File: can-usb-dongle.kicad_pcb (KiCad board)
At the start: 2 copper layers, 30 x 15 mm, 43 parts, among them SW1 SW_PUSH, U1 STM32F302C8T, U2 SN65HVD256, U3 NUF2042XV6, U4 MCP1700, U5 SiP32431, X1 16MHz 10ppm

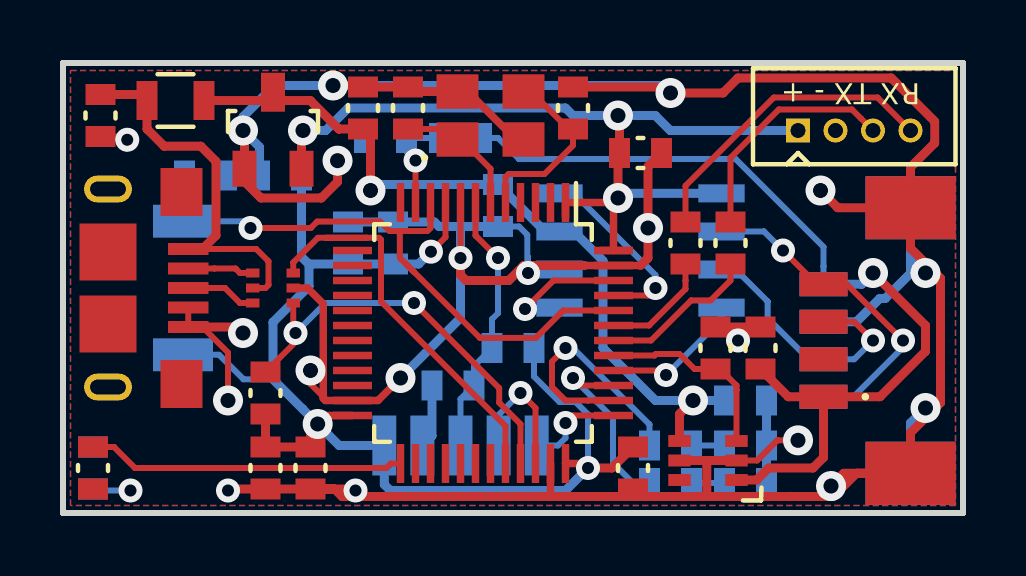
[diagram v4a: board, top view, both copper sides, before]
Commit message: Resolve JTAG pin conflict, add V_BUS_SENSE filter cap
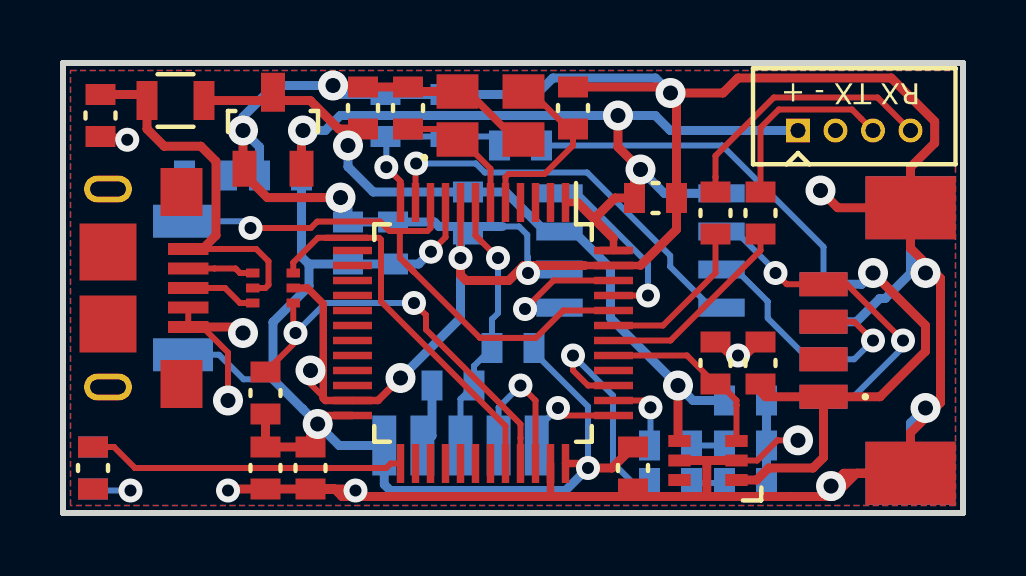
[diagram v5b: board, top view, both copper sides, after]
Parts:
- added C16: 100nF, _std:_0603, B.Cu at (57.8, 39.2)
- moved R3 2.02 mm to (60.2, 40.2)
- moved C3 1.58 mm to (64.8, 42.0)
- moved R10 1.41 mm to (66.8, 42.5)
- moved R11 1.41 mm to (68.2, 42.5)
- moved C9 1.03 mm to (58.5, 42.5)
- moved R4 0.75 mm to (55.8, 39.2), turned to 90 degrees
- moved C14 0.50 mm to (68.2, 47.5)
- moved R9 0.50 mm to (66.8, 47.5)
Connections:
- U1 pad 11: /V_BUS_SENSE -> /CAN_SILENT
- U1 pad 12: Net-(U1-Pad12) -> /V_BUS_SENSE
- U1 pad 40: /CAN_SILENT -> Net-(U1-Pad40)
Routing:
- net /CAN_SILENT: track 4.82 -> 13.7 mm
- net /CAN1_PWR_LED: track 8.28 -> 2.61 mm
- net /V_BUS_SENSE: track 3.37 -> 6.33 mm
- net /V_CAN_BUS: track 32.1 -> 29.7 mm
- net GND: track 158.5 -> 160.9 mm, vias 20 -> 19
- net /UART1_RX: track 3.74 -> 5.42 mm
- net Net-(CONN1-Pad4): track 10.4 -> 8.97 mm
- net /UART1_TX: track 5.28 -> 6.69 mm
- net Net-(CONN1-Pad3): track 7.85 -> 6.43 mm
- net /CAN1_STATUS_LED: track 6.33 -> 7.69 mm
- net /SWDIO: track 4.61 -> 5.11 mm

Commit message: Fix silkscreen text
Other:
- board text added: "CAN to USB RevA"
- board text removed: "CVRA CAN to USB dongle Rev A"
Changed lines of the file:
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@@
     (area 44.899999 37.399999 75.100001 52.600001)
     (thickness 1.6)
-    (drawings 21)
+    (drawings 23)
     (tracks 487)
     (zones 0)
@@
   )
   (setup
-    (last_trace_width 0.3)
+    (last_trace_width 0.2)
     (user_trace_width 0.1524)
     (user_trace_width 0.1524)
@@
       (net 2 GND))
   )
+  (gr_text + (at 69 49.25) (layer F.SilkS)
+    (effects (font (size 1 1) (thickness 0.2)))
+  )
+  (gr_text + (at 69.25 43.75) (layer B.SilkS)
+    (effects (font (size 1 1) (thickness 0.2)) (justify mirror))
+  )
   (gr_line (start 46.3 51.15) (end 45.7 51.15) (layer B.SilkS) (width 0.15))
   (gr_line (start 46 50.85) (end 46.3 51.15) (layer B.SilkS) (width 0.15))
@@
     (effects (font (size 0.8 0.8) (thickness 0.2)) (justify mirror))
   )
-  (gr_text "CVRA CAN to USB dongle Rev A" (at 45.75 38.75 180) (layer B.SilkS)
+  (gr_text "CAN to USB           RevA" (at 45.75 38.75 180) (layer B.SilkS)
     (effects (font (size 0.8 0.8) (thickness 0.15)) (justify left mirror))
   )

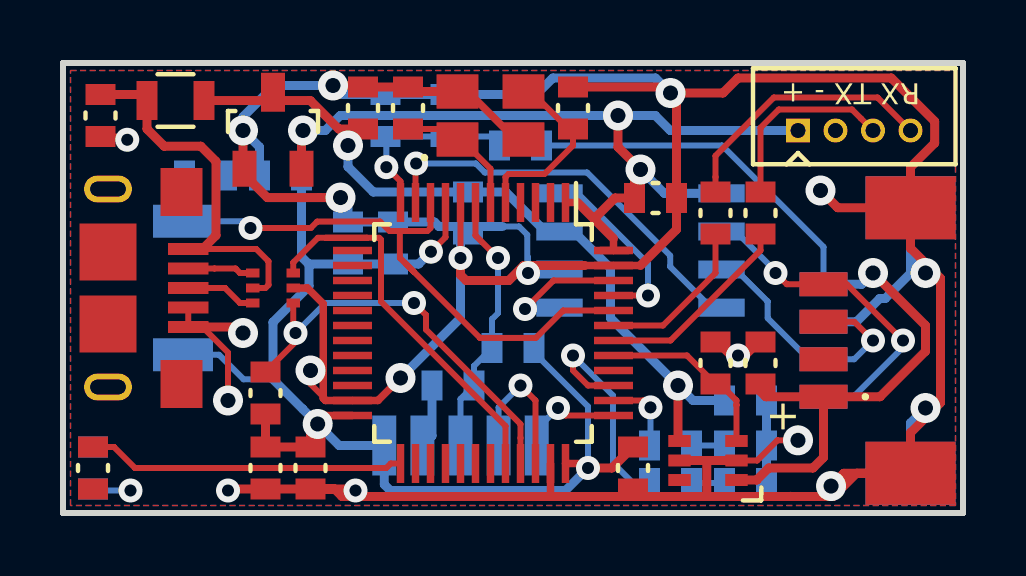
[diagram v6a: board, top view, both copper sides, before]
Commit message: Increase component dinstance on backside for handsoldering
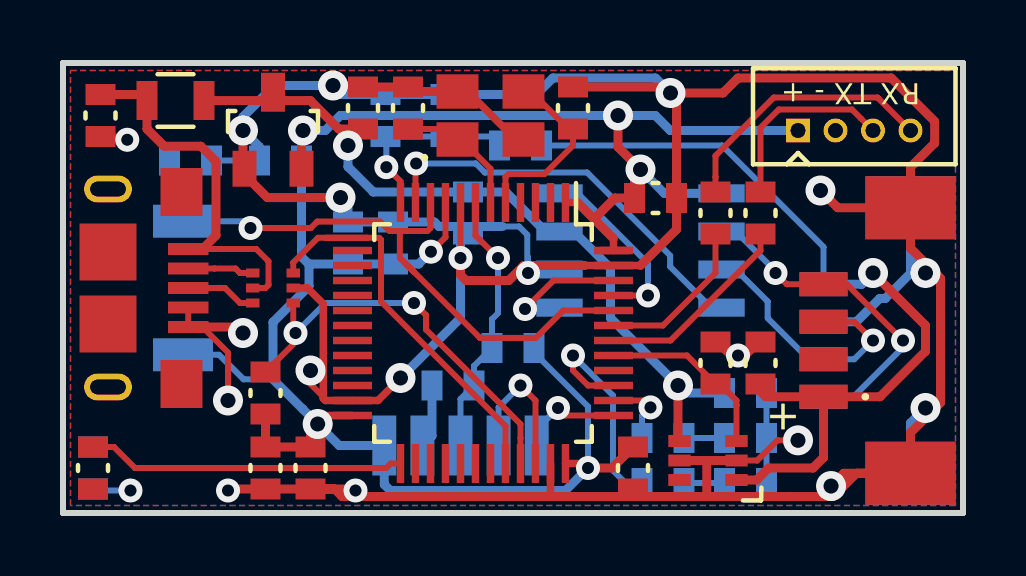
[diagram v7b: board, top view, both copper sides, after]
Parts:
- moved R2 0.71 mm to (49.2, 40.8)
- moved C12 0.50 mm to (52.2, 40.8)
- moved R7 0.35 mm to (65.0, 50.0)
- moved C10 0.25 mm to (67.8, 48.5)
- moved D3 0.25 mm to (67.8, 50.0)
- moved R6 0.25 mm to (65.0, 51.5)
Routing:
- net /BOOT0: track 20.9 -> 21.6 mm
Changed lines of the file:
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@@
     (thickness 1.6)
     (drawings 23)
-    (tracks 487)
+    (tracks 488)
     (zones 0)
     (modules 44)
@@
   )
   (setup
-    (last_trace_width 0.2)
+    (last_trace_width 0.3)
     (user_trace_width 0.1524)
     (user_trace_width 0.1524)
@@
   )
   (module _std:_0603 (layer B.Cu)
-    (at 67.75 48.75)
+    (at 67.75 48.5)
     (fp_text reference C10 (at 0 0) (layer B.SilkS) hide
       (effects (font (size 0.5 0.5) (thickness 0.125)) (justify mirror))
@@
   )
   (module _std:_0603 (layer B.Cu)
-    (at 52.25 41.25 180)
+    (at 52.25 40.75 180)
     (fp_text reference C12 (at 0 0 180) (layer B.SilkS) hide
       (effects (font (size 0.5 0.5) (thickness 0.125)) (justify mirror))
@@
   )
   (module _std:_0603 (layer B.Cu)
-    (at 67.75 50.25 180)
+    (at 67.75 50 180)
     (fp_text reference D3 (at 0 0 180) (layer B.SilkS) hide
       (effects (font (size 0.5 0.5) (thickness 0.125)) (justify mirror))
@@
   )
   (module _std:_0603 (layer B.Cu)
-    (at 49.75 41.25)
+    (at 49.25 40.75)
     (fp_text reference R2 (at 0 0) (layer B.SilkS) hide
       (effects (font (size 0.5 0.5) (thickness 0.125)) (justify mirror))
@@
   )
   (module _std:_0603 (layer B.Cu)
-    (at 65.25 51.5)
+    (at 65 51.5)
     (fp_text reference R6 (at 0 0) (layer B.SilkS) hide
       (effects (font (size 0.5 0.5) (thickness 0.125)) (justify mirror))
@@
   )
   (module _std:_0603 (layer B.Cu)
-    (at 65.25 50.25)
+    (at 65 50)
     (fp_text reference R7 (at 0 0) (layer B.SilkS) hide
       (effects (font (size 0.5 0.5) (thickness 0.125)) (justify mirror))
@@
   (gr_line (start 67.95 51.5) (end 67.6 51.8) (layer B.SilkS) (width 0.15))
   (gr_line (start 67.6 51.2) (end 67.95 51.5) (layer B.SilkS) (width 0.15))
-  (gr_line (start 67.6 50.55) (end 67.95 50.25) (layer B.SilkS) (width 0.15))
-  (gr_line (start 67.6 49.95) (end 67.6 50.55) (layer B.SilkS) (width 0.15))
-  (gr_line (start 67.95 50.25) (end 67.6 49.95) (layer B.SilkS) (width 0.15))
+  (gr_line (start 67.6 50.3) (end 67.95 50) (layer B.SilkS) (width 0.15))
+  (gr_line (start 67.6 49.7) (end 67.6 50.3) (layer B.SilkS) (width 0.15))
+  (gr_line (start 67.95 50) (end 67.6 49.7) (layer B.SilkS) (width 0.15))
   (gr_text CAN (at 70.25 51.5 180) (layer B.SilkS)
     (effects (font (size 0.8 0.8) (thickness 0.2)) (justify mirror))
   )
-  (gr_text PWR (at 70.25 50.25 180) (layer B.SilkS)
+  (gr_text PWR (at 70.25 50 180) (layer B.SilkS)
     (effects (font (size 0.8 0.8) (thickness 0.2)) (justify mirror))
   )
@@
   (segment (start 61.769981 50.869981) (end 61.75 50.85) (width 0.25) (layer F.Cu) (net 1))
   (via (at 62.5 51) (size 0.8) (drill 0.4) (layers F.Cu B.Cu) (net 1))
+  (segment (start 51.55 40.75) (end 51.55 40.3) (width 0.3) (layer B.Cu) (net 2))
+  (segment (start 51.55 40.3) (end 51 39.75) (width 0.3) (layer B.Cu) (net 2))
+  (segment (start 49.95 40.75) (end 51.55 40.75) (width 0.2) (layer B.Cu) (net 2))
+  (segment (start 68.45 50) (end 68.45 51.5) (width 0.2) (layer B.Cu) (net 2))
+  (segment (start 68.45 48.5) (end 68.45 50) (width 0.2) (layer B.Cu) (net 2))
   (segment (start 67.5 47.25) (end 67.2 47.25) (width 0.2) (layer F.Cu) (net 2))
   (segment (start 67.2 47.25) (end 66.75 46.8) (width 0.2) (layer F.Cu) (net 2))
@@
   (segment (start 55.5 48.75) (end 56.25 48) (width 0.25) (layer F.Cu) (net 2))
   (via (at 56.25 48) (size 1) (drill 0.5) (layers F.Cu B.Cu) (net 2))
-  (segment (start 50.45 41.25) (end 51.55 41.25) (width 0.3) (layer B.Cu) (net 2))
   (segment (start 62 38.3) (end 65.05 38.3) (width 0.3) (layer F.Cu) (net 2))
   (segment (start 65.05 38.3) (end 65.25 38.5) (width 0.3) (layer F.Cu) (net 2))
@@
   (segment (start 51 39.292894) (end 52.042894 38.25) (width 0.3) (layer B.Cu) (net 2))
   (segment (start 52.042894 38.25) (end 54 38.25) (width 0.3) (layer B.Cu) (net 2))
-  (segment (start 51.55 41.25) (end 51.55 40.3) (width 0.3) (layer B.Cu) (net 2))
-  (segment (start 51.55 40.3) (end 51 39.75) (width 0.3) (layer B.Cu) (net 2))
   (via (at 51 39.75) (size 1) (drill 0.5) (layers F.Cu B.Cu) (net 2))
   (segment (start 70.35 46.125) (end 71.45 46.125) (width 0.3) (layer B.Cu) (net 2))
@@
   (segment (start 74.250011 48.824989) (end 73.25 49.825) (width 0.3) (layer F.Cu) (net 2))
   (segment (start 73.25 49.825) (end 73.25 51.175) (width 0.3) (layer F.Cu) (net 2))
-  (segment (start 68.45 50.25) (end 68.45 51.5) (width 0.3) (layer B.Cu) (net 2))
-  (segment (start 68.45 48.75) (end 68.45 50.25) (width 0.3) (layer B.Cu) (net 2))
   (segment (start 64 51.95) (end 61.305065 51.95) (width 0.3) (layer F.Cu) (net 2))
   (segment (start 61.305065 51.95) (end 54.3 51.95) (width 0.3) (layer F.Cu) (net 2))
@@
   (segment (start 62 40.25) (end 62 39.7) (width 0.2) (layer F.Cu) (net 5))
   (segment (start 60.025 38.4) (end 59.9 38.4) (width 0.2) (layer F.Cu) (net 5))
-  (segment (start 67.05 48.75) (end 66 48.75) (width 0.3) (layer B.Cu) (net 6))
-  (segment (start 66 48.75) (end 65.5 48.25) (width 0.3) (layer B.Cu) (net 6))
+  (segment (start 67.05 48.5) (end 65.75 48.5) (width 0.3) (layer B.Cu) (net 6))
+  (segment (start 65.75 48.5) (end 65.5 48.25) (width 0.3) (layer B.Cu) (net 6))
   (segment (start 65.5 48.25) (end 65.5 50.04972) (width 0.3) (layer F.Cu) (net 6))
   (segment (start 65.5 50.04972) (end 65.55004 50.09976) (width 0.3) (layer F.Cu) (net 6))
@@
   (segment (start 47.4 51) (end 55.775 51) (width 0.2) (layer F.Cu) (net 13))
   (segment (start 55.925 50.85) (end 56.25 50.85) (width 0.2) (layer F.Cu) (net 13))
+  (segment (start 48.55 40.75) (end 48.55 42.325) (width 0.2) (layer B.Cu) (net 14))
+  (segment (start 48.55 42.325) (end 49 42.775) (width 0.2) (layer B.Cu) (net 14))
   (segment (start 60.760083 46.663999) (end 58.900001 46.663999) (width 0.2) (layer F.Cu) (net 14))
   (segment (start 63.35 45.75) (end 61.674082 45.75) (width 0.2) (layer F.Cu) (net 14))
@@
   (segment (start 56.229049 43.100001) (end 56.229049 43.993047) (width 0.2) (layer F.Cu) (net 14))
   (segment (start 56.229049 43.993047) (end 56.689849 44.453847) (width 0.2) (layer F.Cu) (net 14))
-  (segment (start 49.05 41.25) (end 49.05 42.725) (width 0.2) (layer B.Cu) (net 14))
   (segment (start 49.05 42.725) (end 49 42.775) (width 0.2) (layer B.Cu) (net 14))
   (segment (start 49 42.775) (end 51.025 42.775) (width 0.2) (layer B.Cu) (net 14))
@@
   (segment (start 53.500001 43.324999) (end 55.137313 43.324999) (width 0.2) (layer F.Cu) (net 25))
   (segment (start 62 47.25) (end 63.332834 48.582834) (width 0.2) (layer B.Cu) (net 26))
-  (segment (start 63.332834 48.582834) (end 63.332834 50.832834) (width 0.2) (layer B.Cu) (net 26))
-  (segment (start 63.332834 50.832834) (end 64 51.5) (width 0.2) (layer B.Cu) (net 26))
-  (segment (start 64 51.5) (end 64.55 51.5) (width 0.2) (layer B.Cu) (net 26))
+  (segment (start 63.332834 48.582834) (end 63.332834 51.082834) (width 0.2) (layer B.Cu) (net 26))
+  (segment (start 63.332834 51.082834) (end 63.75 51.5) (width 0.2) (layer B.Cu) (net 26))
+  (segment (start 63.75 51.5) (end 64.3 51.5) (width 0.2) (layer B.Cu) (net 26))
   (segment (start 63.35 48.25) (end 62.5 48.25) (width 0.2) (layer F.Cu) (net 26))
   (segment (start 62.5 48.25) (end 62 47.75) (width 0.2) (layer F.Cu) (net 26))
   (segment (start 62 47.75) (end 62 47.25) (width 0.2) (layer F.Cu) (net 26))
   (via (at 62 47.25) (size 0.8) (drill 0.4) (layers F.Cu B.Cu) (net 26))
+  (segment (start 64.3 50) (end 64.3 49.261566) (width 0.2) (layer B.Cu) (net 27))
+  (segment (start 64.3 49.261566) (end 64.582087 48.979479) (width 0.2) (layer B.Cu) (net 27))
   (via (at 64.582087 48.979479) (size 0.8) (drill 0.4) (layers F.Cu B.Cu) (net 27))
   (segment (start 64.352608 48.75) (end 64.582087 48.979479) (width 0.2) (layer F.Cu) (net 27))
-  (segment (start 64.582087 48.979479) (end 64.582087 50.217913) (width 0.2) (layer B.Cu) (net 27))
-  (segment (start 64.582087 50.217913) (end 64.55 50.25) (width 0.2) (layer B.Cu) (net 27))
   (segment (start 63.35 48.75) (end 64.352608 48.75) (width 0.2) (layer F.Cu) (net 27))
   (segment (start 68.25 41.8) (end 68.25 39.659998) (width 0.2) (layer F.Cu) (net 28))
@@
   (segment (start 46.05 51.75) (end 46 51.7) (width 0.2) (layer B.Cu) (net 46))
   (via (at 47.25 51.75) (size 0.8) (drill 0.4) (layers F.Cu B.Cu) (net 46))
-  (segment (start 65.95 51.5) (end 67.05 51.5) (width 0.2) (layer B.Cu) (net 47))
-  (segment (start 65.95 50.25) (end 67.05 50.25) (width 0.2) (layer B.Cu) (net 48))
+  (segment (start 65.7 51.5) (end 67.05 51.5) (width 0.2) (layer B.Cu) (net 47))
+  (segment (start 65.7 50) (end 67.05 50) (width 0.2) (layer B.Cu) (net 48))
   (segment (start 70.35 48.625) (end 68.425 48.625) (width 0.3) (layer F.Cu) (net 53))
   (segment (start 68.425 48.625) (end 68.25 48.45) (width 0.3) (layer F.Cu) (net 53))
